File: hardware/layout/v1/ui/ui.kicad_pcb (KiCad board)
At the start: 4 copper layers, 13.8 x 40.5 mm, 25 parts, among them J1 Main board, J2 OLED, SW1 RST/WIFI, SW2 PAGE, U1 74AHCT1G125

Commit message: replace SS16 Schottky diodes with SS34
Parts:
- D1: value RGB STATUS -> SK6805-EC15
- D2: value RGB NET -> SK6805-EC15
- D3: value RGB SENS -> SK6805-EC15
- J1: value Main board -> FPC-05F-8PH20
- SW1: value RST/WIFI -> B3U-1000P
- SW2: value PAGE -> B3U-1000P

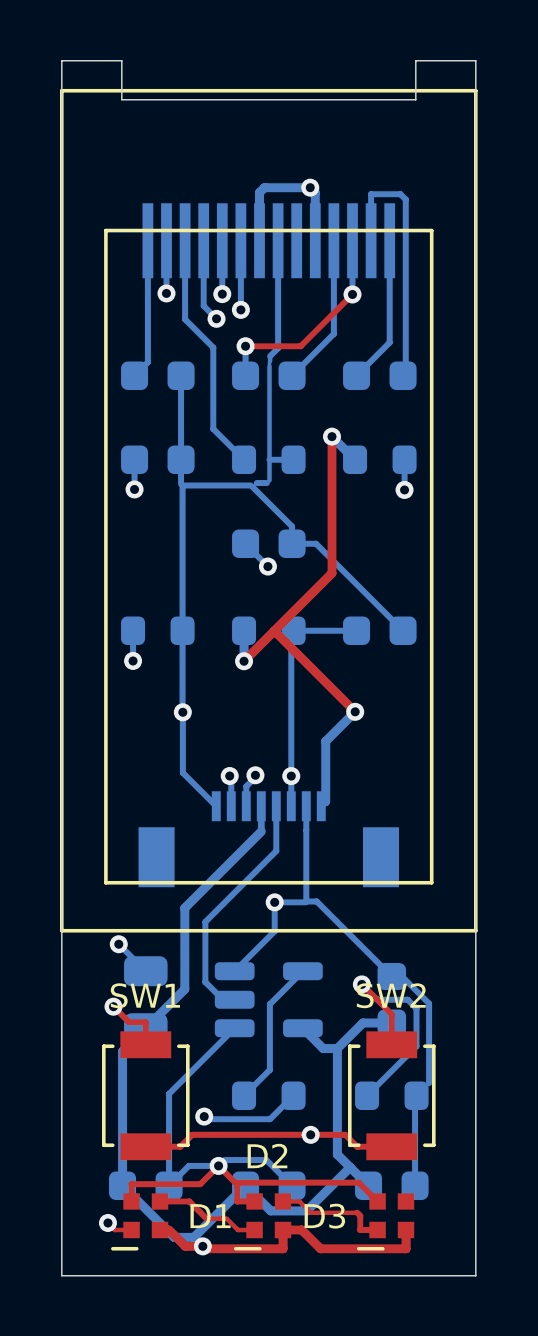
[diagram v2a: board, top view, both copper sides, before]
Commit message: extend GND track joints on main board to fully seat on pads/vias
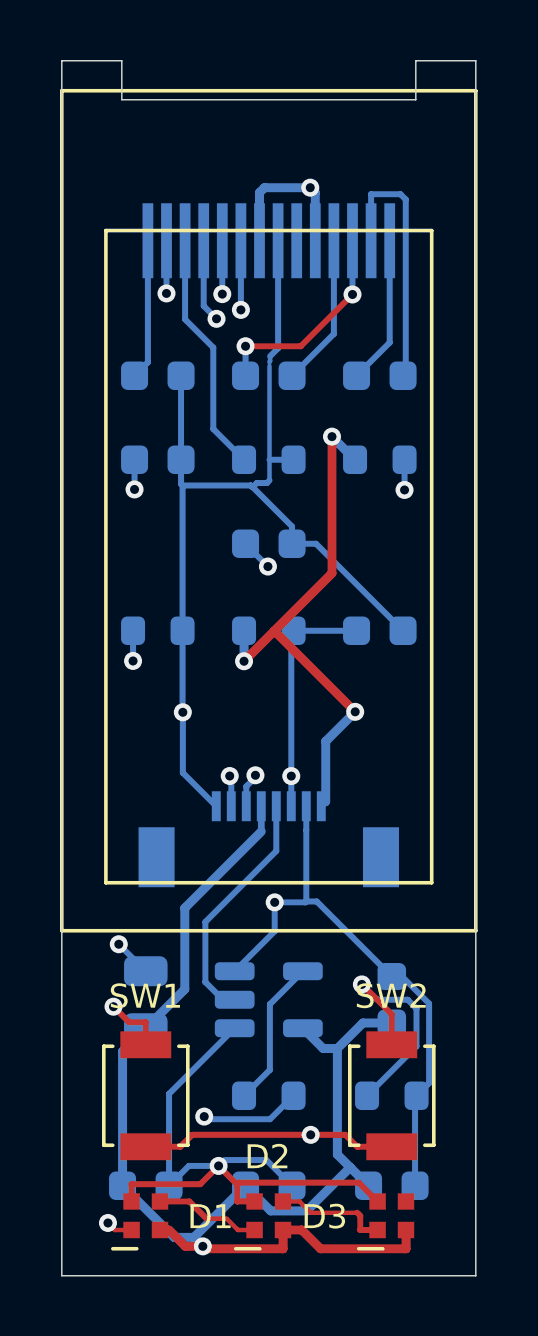
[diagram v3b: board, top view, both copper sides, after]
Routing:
- net GND: track 74.0 -> 75.4 mm
